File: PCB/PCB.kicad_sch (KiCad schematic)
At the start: 38 parts, among them J1 USB_C_Receptacle_USB2.0_16P, SW1 SW_Push, SW2 SW_Push, U1 RP2040, U2 USBLC6-2SC6, U3 NCP1117ST33T3G, U4 W25Q32JVSS, U5 Conn, Y1 Crystal_GND24

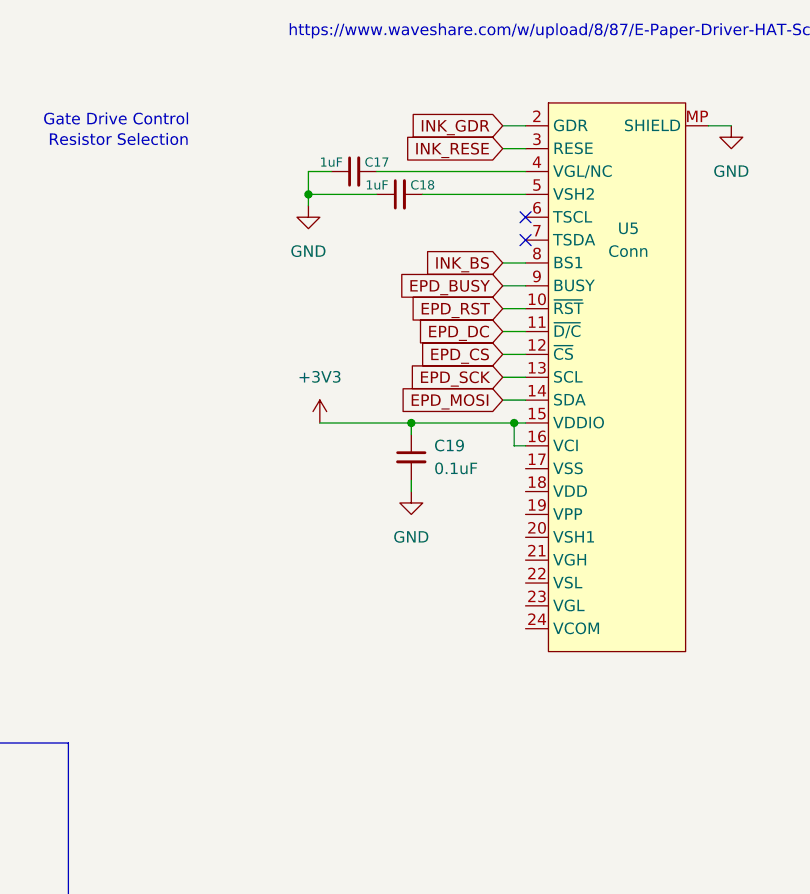
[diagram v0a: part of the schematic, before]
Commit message: finished wiring the eink connector
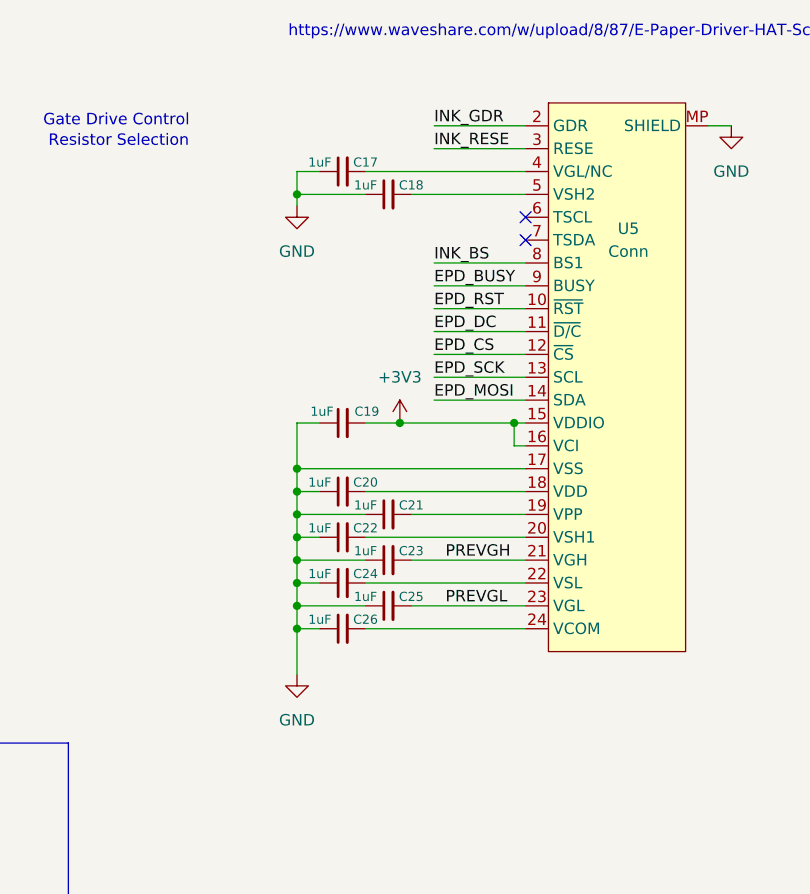
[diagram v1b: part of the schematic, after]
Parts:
- added C20, C21, C22, C23, C24, C25, C26: 1uF, symbol Device:C_Small
- C19: value 0.1uF -> 1uF
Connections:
- net +3V3: now also C19.2; no longer C19.1
- net GND: now also C19.1, U5.17 (VSS), C20.1, C21.1, C22.1, C23.1, C24.1, C25.1, C26.1; no longer C19.2
- net at U5.18 (VDD): now also C20.2
- net at U5.19 (VPP): now also C21.2
- net at U5.20 (VSH1): now also C22.2
- net PREVGH: now reaches U5.21 (VGH)
- net PREVGH: now also C23.2
- net at U5.22 (VSL): now also C24.2
- net PREVGL: now reaches U5.23 (VGL)
- net PREVGL: now also C25.2
- net at U5.24 (VCOM): now also C26.2
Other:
- moved on the sheet: C17, C18, C19

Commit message: wired the eink mosfet logic!
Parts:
- added C27, C28: 4.7uF, symbol Device:C
- added D2, D3, D4: MBR0530, Diode_SMD:D_SOD-123, symbol Diode:MBR0530
- added L2: 68uH, symbol Device:L
- added Q2: IRLML2060, Package_TO_SOT_SMD:SOT-23, symbol Transistor_FET:IRLML2060
- added R11: 10K, symbol Device:R
- added R12: 0.47, symbol Device:R
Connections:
- net +3V3: now also C28.2, L2.1
- net GND: now also C28.1, D4.1 (K), R11.2, R12.2
- net PREVGH: now also D2.1 (K)
- net PREVGL: now also D3.2 (A)
- net INK_BS renamed BS
- net INK_GDR renamed GDR
- net GDR: now also Q2.1 (G), R11.1
- net INK_RESE renamed RESE
- net RESE: now also Q2.2 (S), R12.1
- new net: C27.2, D2.2 (A), L2.2, Q2.3 (D)
- new net: C27.1, D3.1 (K), D4.2 (A)
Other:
- note added: "Bus Select"
- note added: "Busy Detect"
- moved on the sheet: C1, C10, C11, C12, C13, C14, C15, C16, C17, C18, C19, C2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

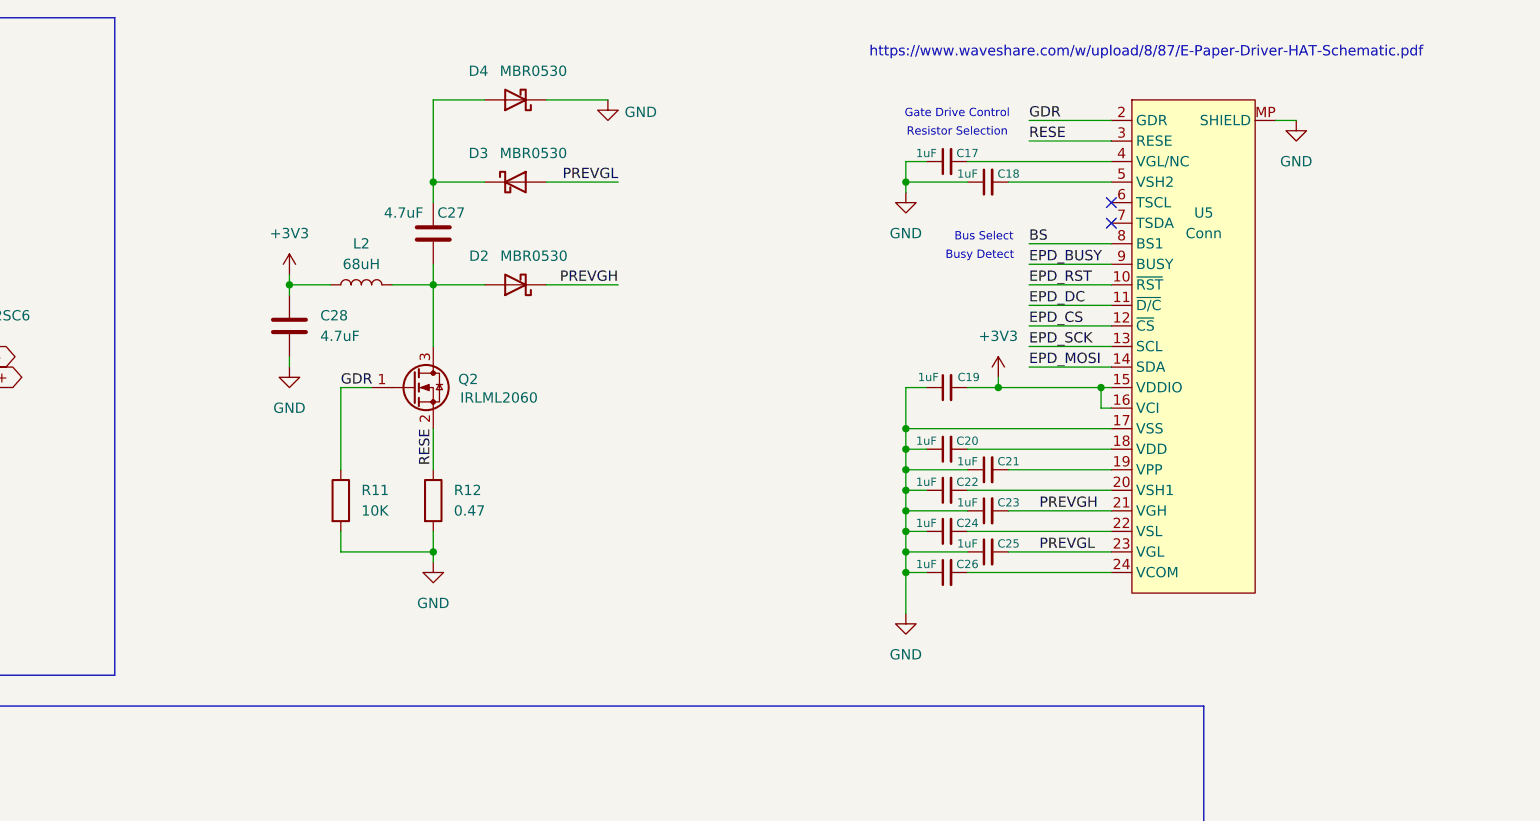
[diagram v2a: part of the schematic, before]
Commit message: cleaning up the e-ink wiring, fixing BS too!
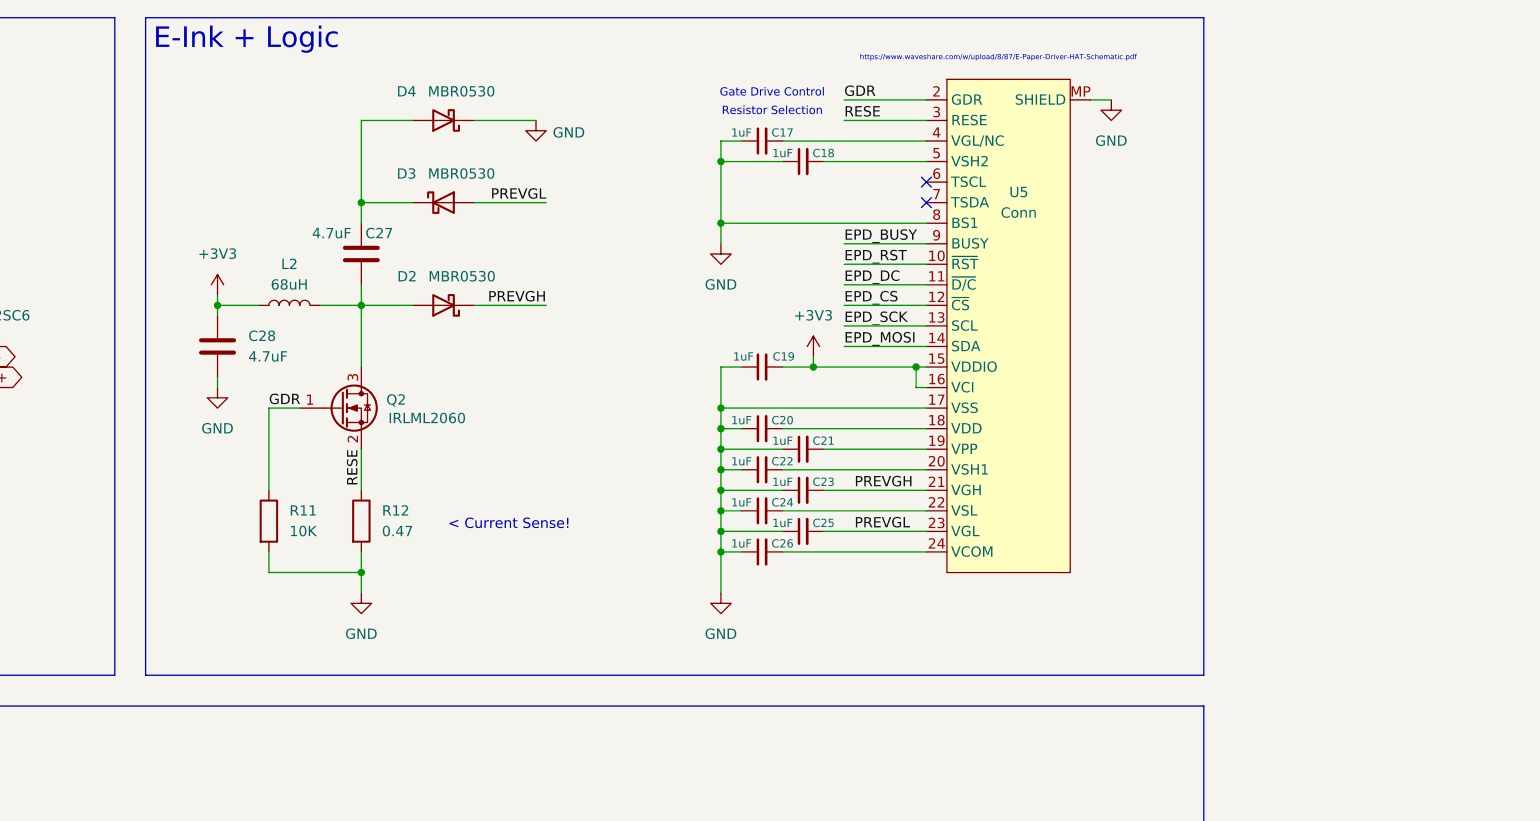
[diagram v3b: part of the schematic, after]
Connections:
- net BS is gone; now on net GND: U5.8 (BS1)
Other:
- note added: "< Current Sense!"
- note removed: "Bus Select"
- note removed: "Busy Detect"
- moved on the sheet: C17, C18, C19, C20, C21, C22, C23, C24, C25, C26, C27, C28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

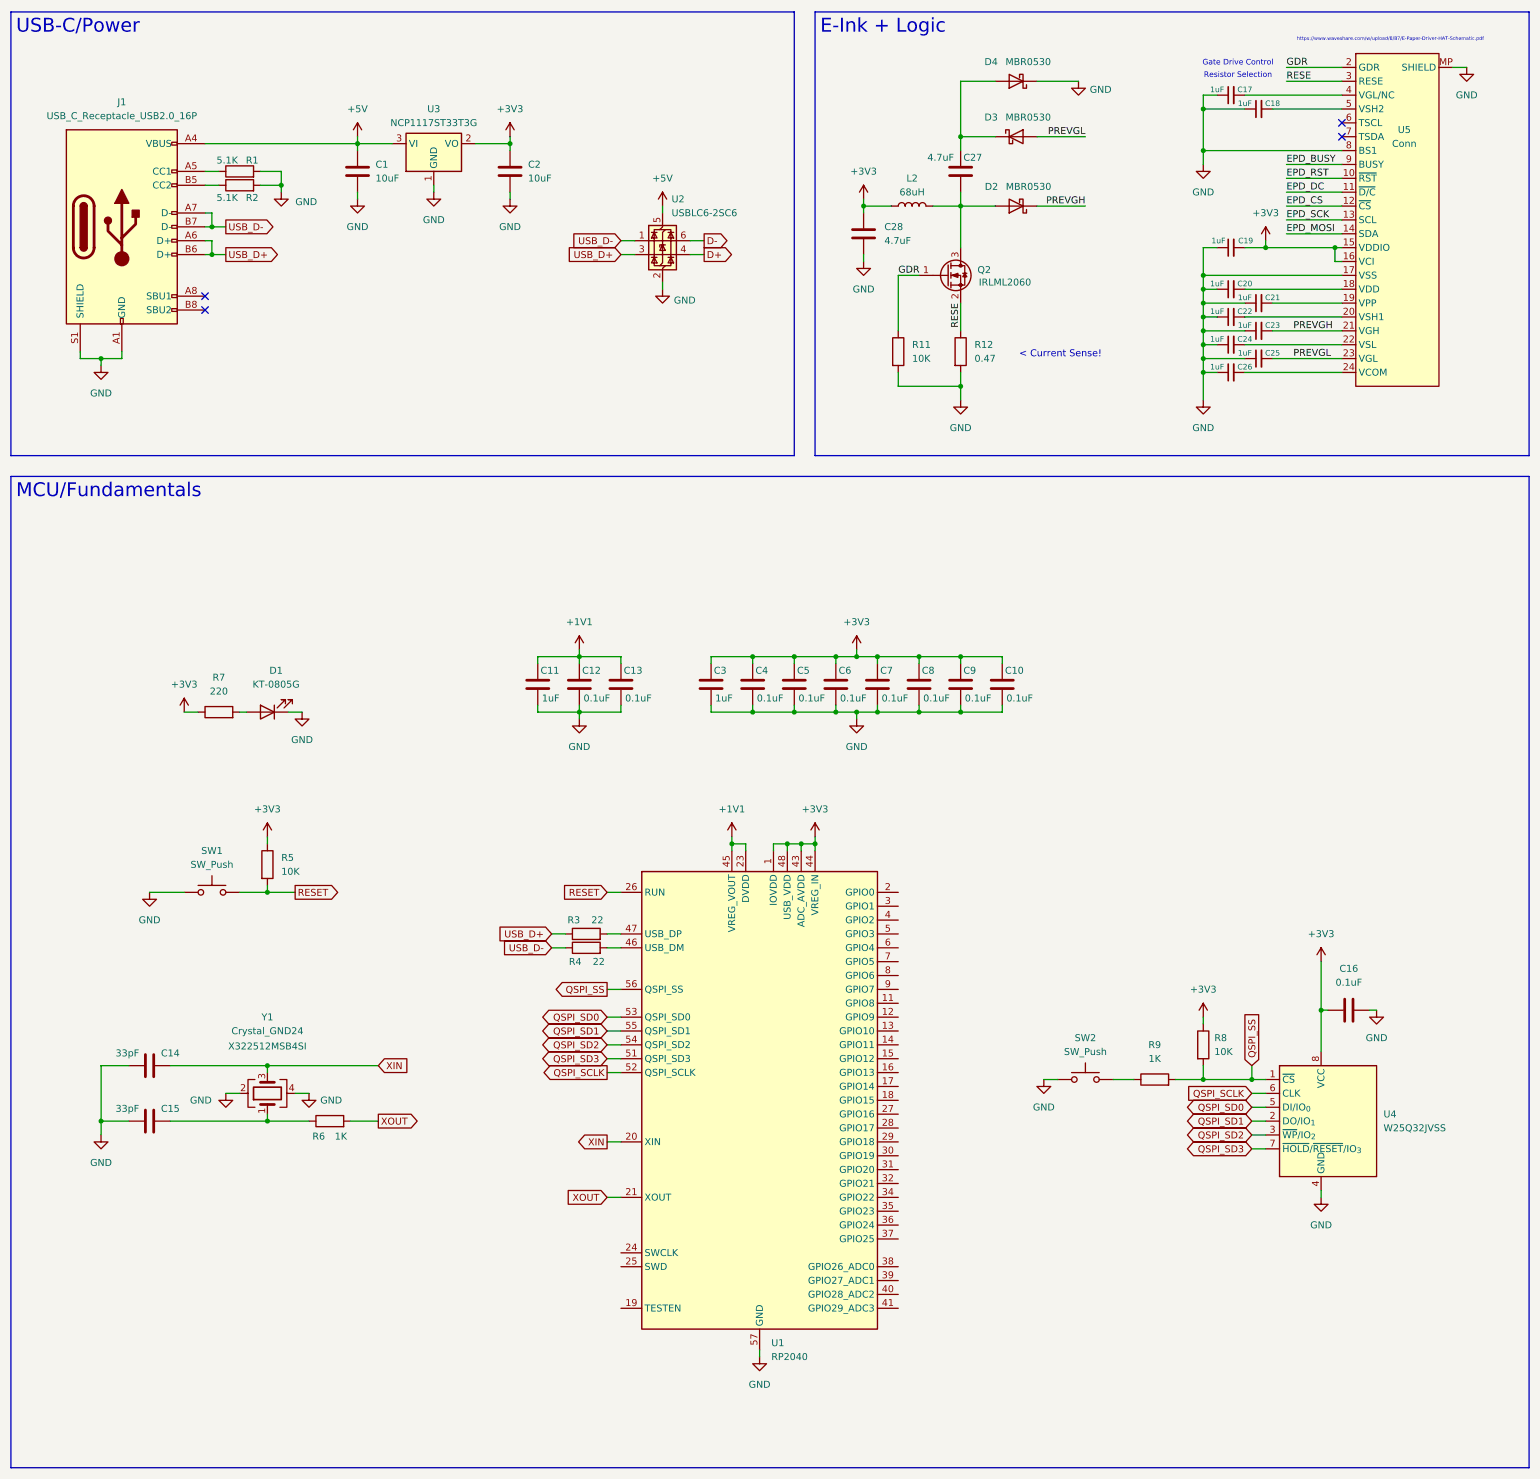
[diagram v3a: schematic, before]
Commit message: finished wiring the eink
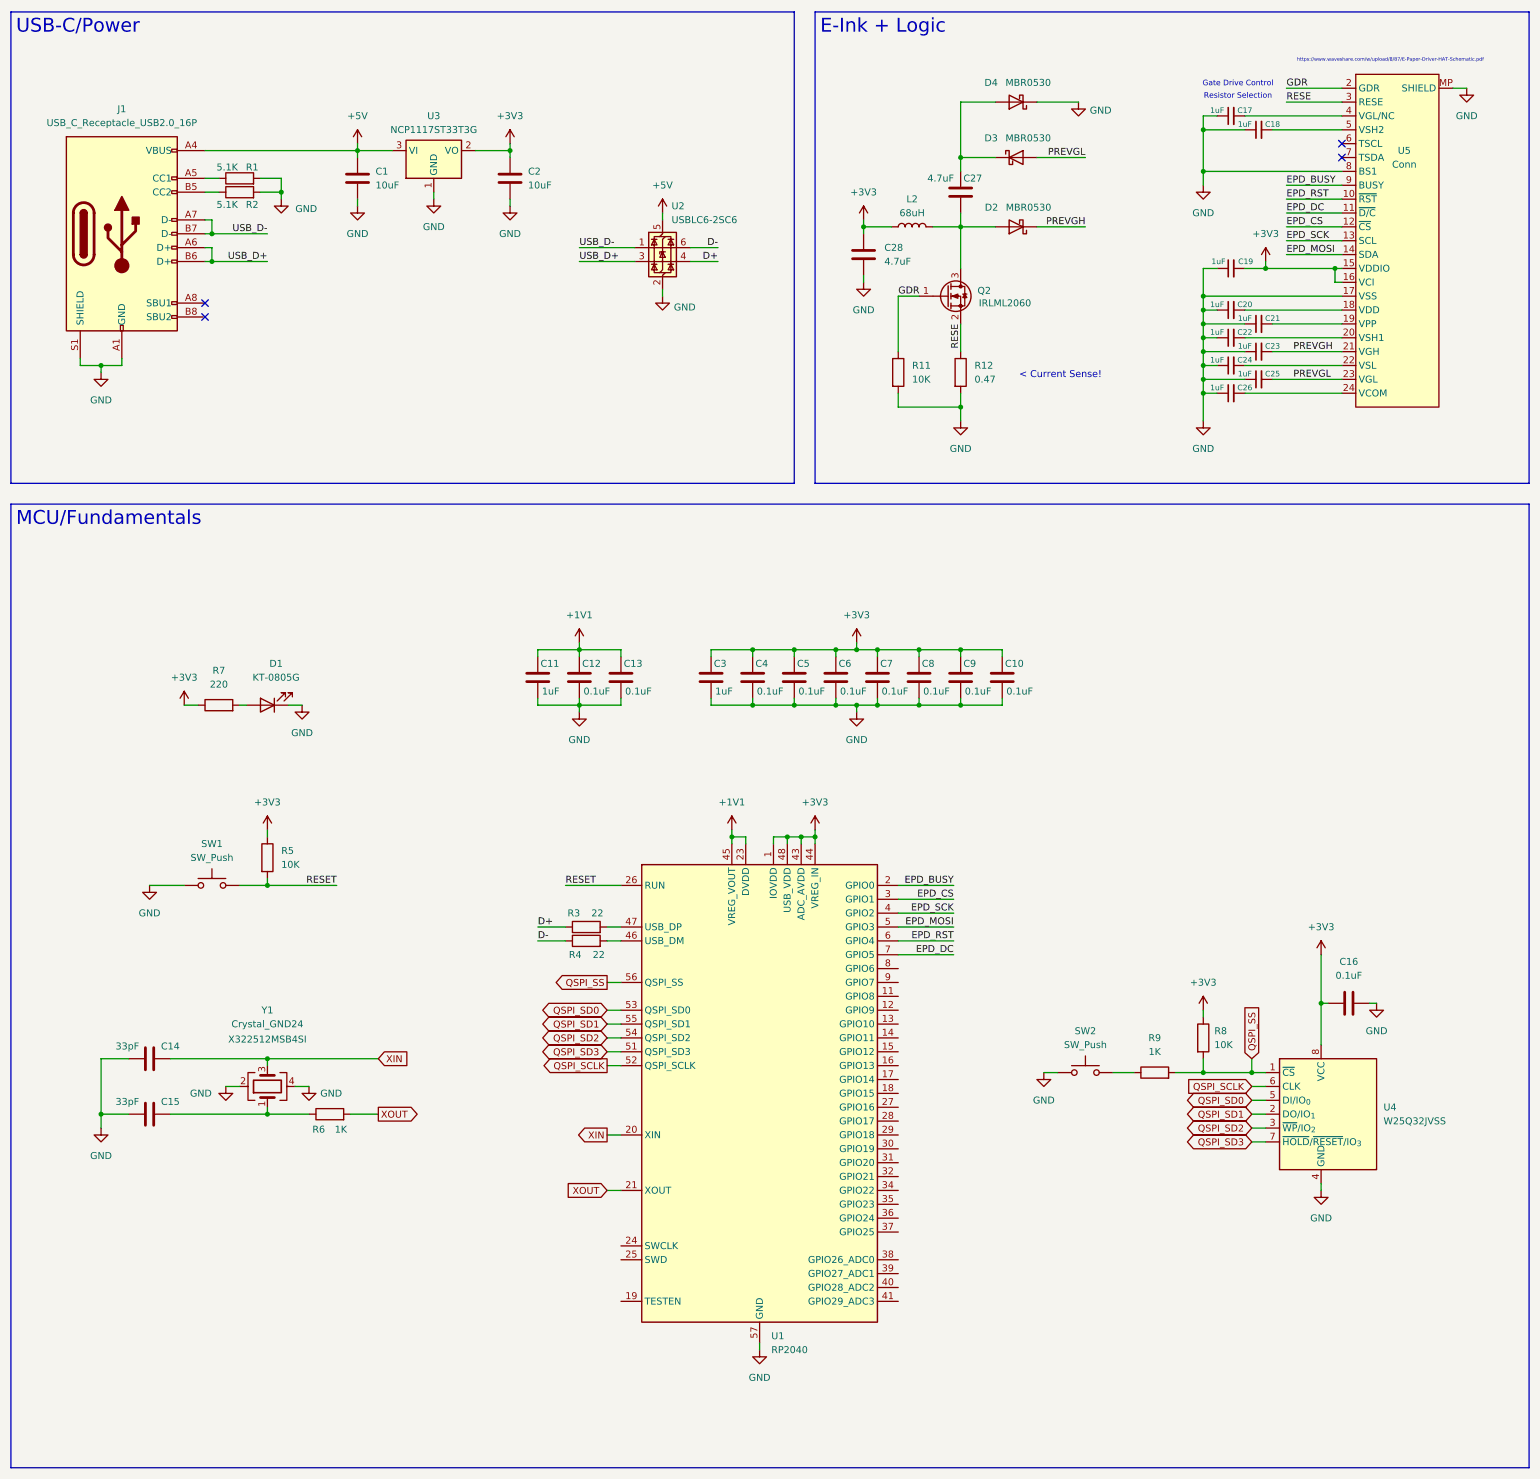
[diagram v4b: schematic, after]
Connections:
- net D+: now also R3.1
- net D-: now also R4.1
- net EPD_BUSY: now also U1.2 (GPIO0)
- net EPD_CS: now also U1.3 (GPIO1)
- net EPD_DC: now also U1.7 (GPIO5)
- net EPD_MOSI: now also U1.5 (GPIO3)
- net EPD_RST: now also U1.6 (GPIO4)
- net EPD_SCK: now also U1.4 (GPIO2)
- net USB_D+: no longer R3.1
- net USB_D-: no longer R4.1
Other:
- moved on the sheet: C1, C10, C11, C12, C13, C14, C15, C16, C17, C18, C19, C2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
